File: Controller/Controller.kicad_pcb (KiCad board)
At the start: 2 copper layers, 50.5 x 20.1 mm, 15 parts, among them J1 Power, J2 Track, J3 DCC, U1 LM7805_TO220, U2 LMD18200T

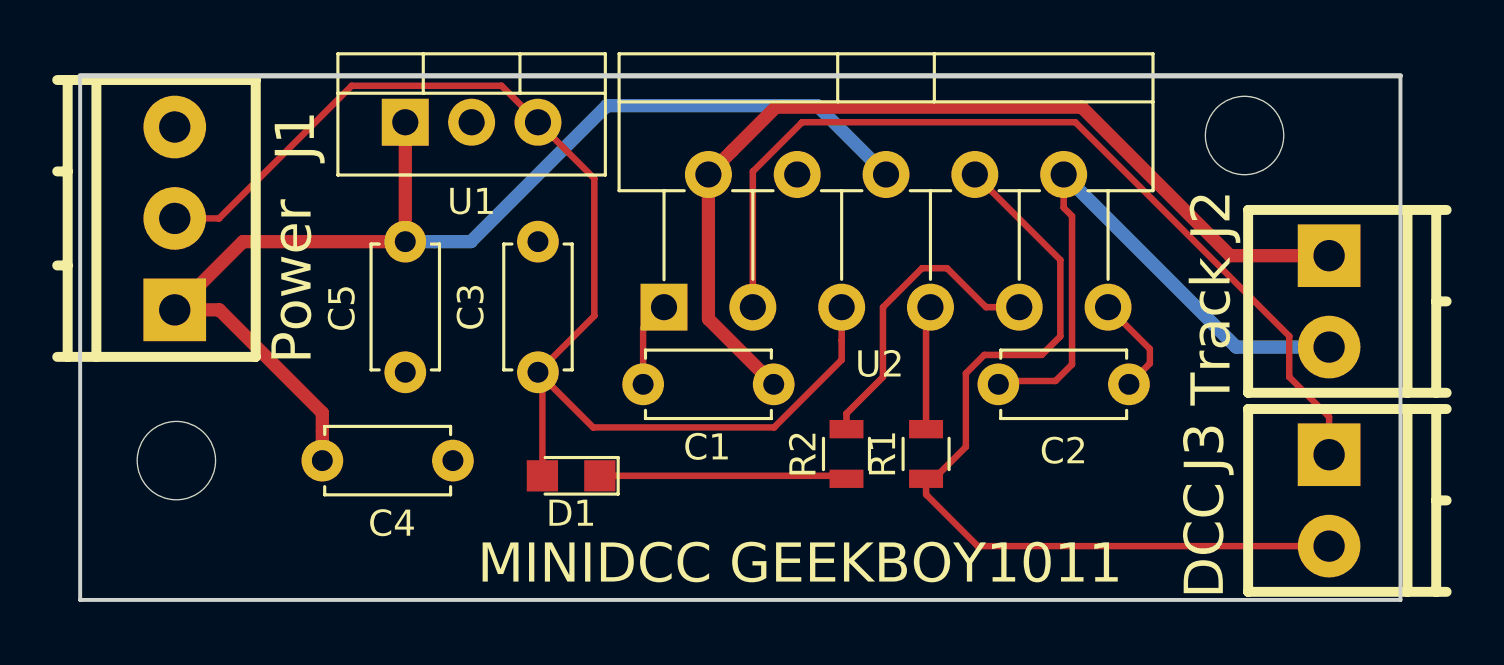
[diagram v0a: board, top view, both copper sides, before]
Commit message: Fixed wrong foot print selection for large filter capacitor Adjusted silkscreen mask
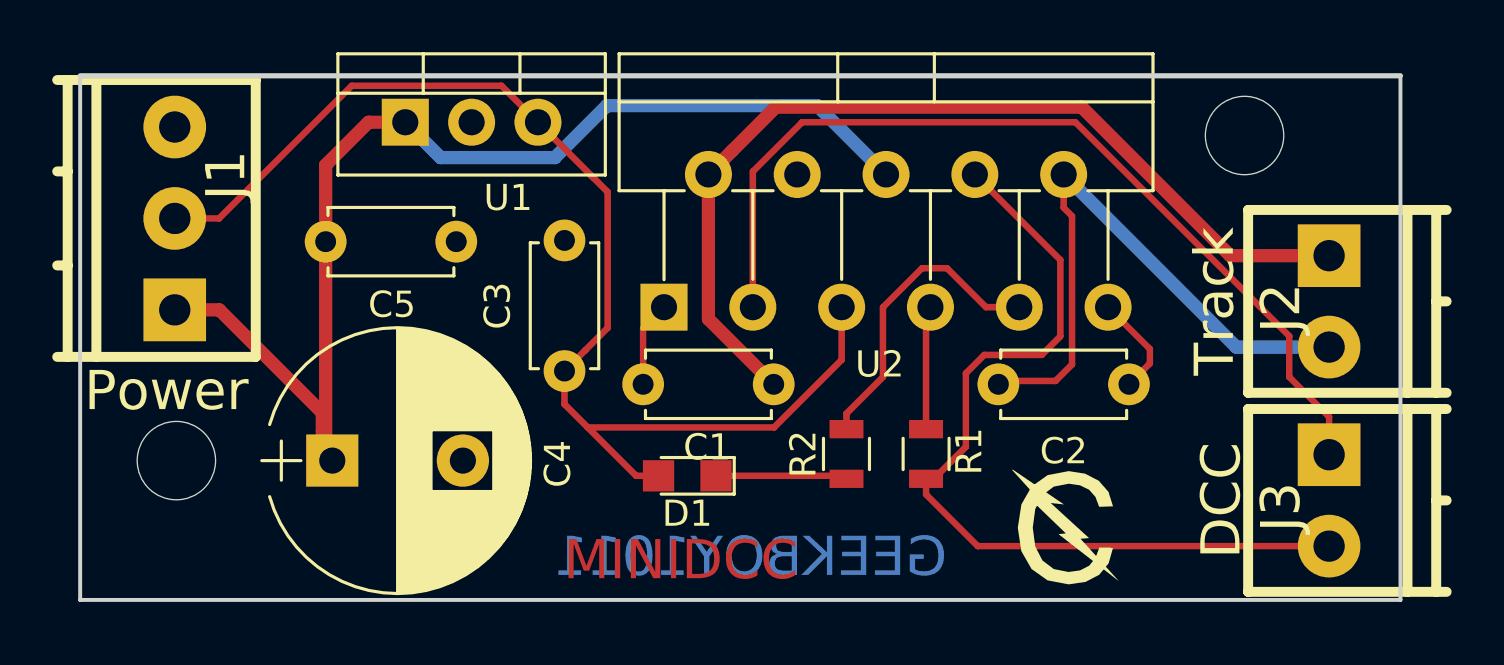
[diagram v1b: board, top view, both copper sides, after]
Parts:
- added CemeLogo: G***, Geekboy:cememod.mod, F.Cu at (113.9, 93.5)
- C4: footprint Capacitors_THT:C_Disc_D4.7mm_W2.5mm_P5.00mm -> Capacitors_THT:CP_Radial_D10.0mm_P5.00mm
- moved D1 4.45 mm to (99.4, 91.5)
- moved C5 3.05 mm to (85.6, 82.5), turned to 0 degrees
- moved C3 1.02 mm to (94.7, 87.5)
- moved C4 0.38 mm to (85.9, 90.9)
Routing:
- net Net-(D1-Pad1): track 9.49 -> 5.04 mm
- net +5V: track 47.6 -> 46.9 mm
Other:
- board text added: "GEEKBOY1011"
- board text added: "MINIDCC"
- board text removed: "MINIDCC GEEKBOY1011"

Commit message: Fixed shortcomings of MINIDCC booster board.
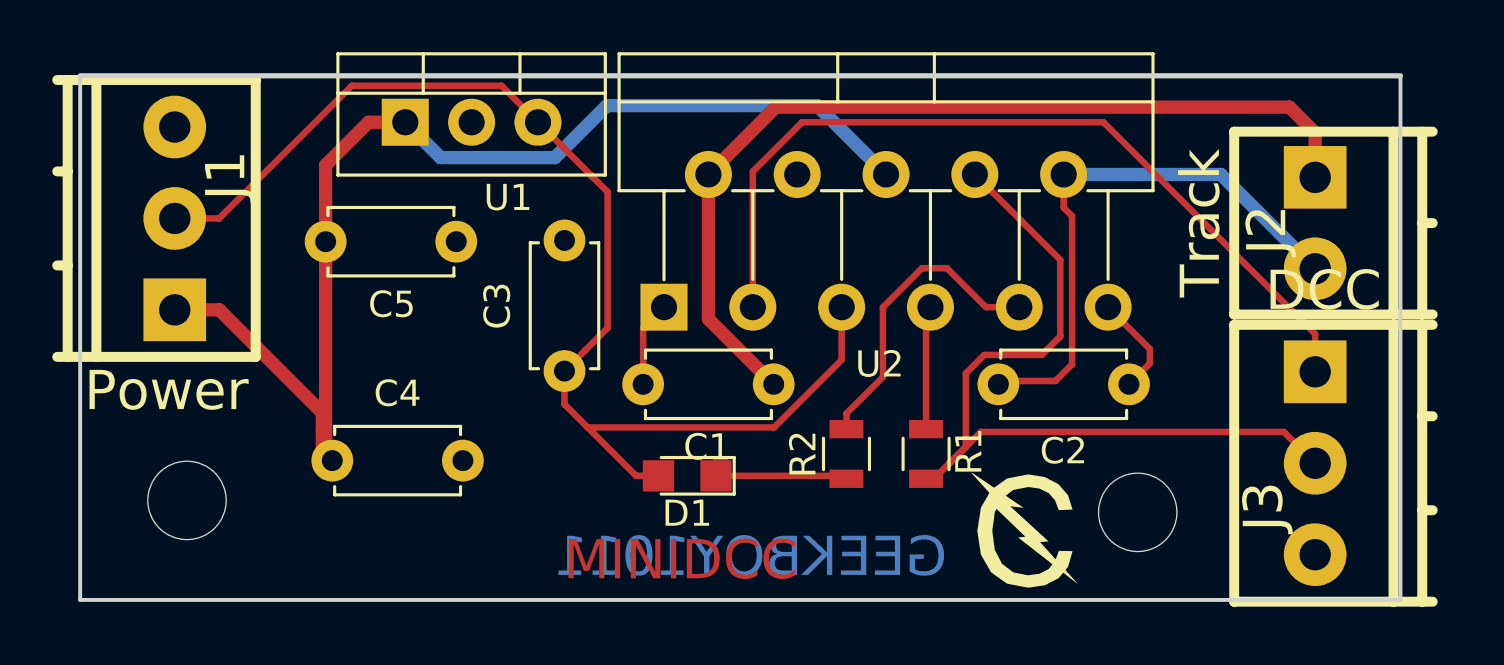
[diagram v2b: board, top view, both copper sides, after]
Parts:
- C4: footprint Capacitors_THT:CP_Radial_D10.0mm_P5.00mm -> Capacitors_THT:C_Disc_D4.7mm_W2.5mm_P5.00mm
- J1: footprint w_conn_pt-1,5:pt_1,5-3-3,5-h -> Geekboy:pt_1,5-3-3,5-h
- J2: footprint w_conn_pt-1,5:pt_1,5-2-3,5-h -> Geekboy:pt_1,5-2-3,5-h
- J3: footprint w_conn_pt-1,5:pt_1,5-2-3,5-h -> Geekboy:pt_1,5-3-3,5-h
- moved ? 15.0 mm to (116.7, 92.9)
- moved J2 3.04 mm to (124.2, 81.8)
- moved ? 1.58 mm to (80.3, 92.5)
- moved CemeLogo 1.55 mm to (112.4, 93.6)
- moved J3 1.52 mm to (124.2, 91.0)
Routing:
- net /Direction: track 35.1 -> 32.3 mm
- net /Current_Sense: track 33.4 -> 31.6 mm
- net /Track2: track 23.9 -> 22.1 mm
- net /Track1: track 36.3 -> 35.5 mm

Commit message: Added silk screen text. Fixed fubars from last commit.
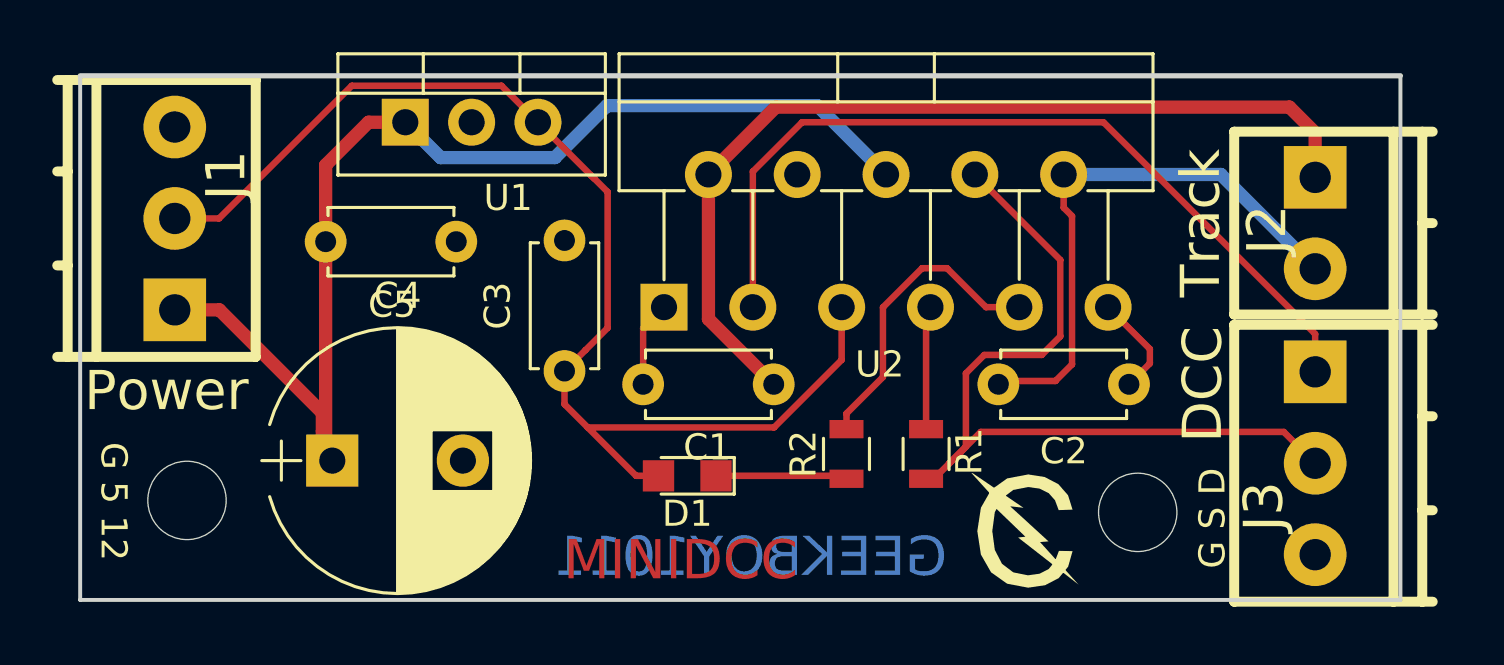
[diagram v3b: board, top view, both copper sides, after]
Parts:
- C4: footprint Capacitors_THT:C_Disc_D4.7mm_W2.5mm_P5.00mm -> Capacitors_THT:CP_Radial_D10.0mm_P5.00mm
- turned ? to 90 degrees
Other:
- board text added: "G 5 12"
- board text added: "G S D"
